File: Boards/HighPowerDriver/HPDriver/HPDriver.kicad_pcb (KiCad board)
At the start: 4 copper layers, 100 parts, among them J1 USB_B_Mini, J2 60V_In, J3 Coils, J4 Screw_Terminal_01x06, J5 AVR-ISP-6, Q10 IRF9530, Q11 BC817, Q12 BC817, Q13 BC817, Q14 BC817, Q9 BC817, SW1 SW_Push, U1 LM5009MM, U10 ATtiny2313A-SU, U2 TMC262, U3 FT230XS, U4 SFH617A-1, U5 SFH617A-1, U6 TLP118, U7 LTV-827S, U8 LTV-827S, U9 74HC14, X1 16MHz, Y1 20MHz

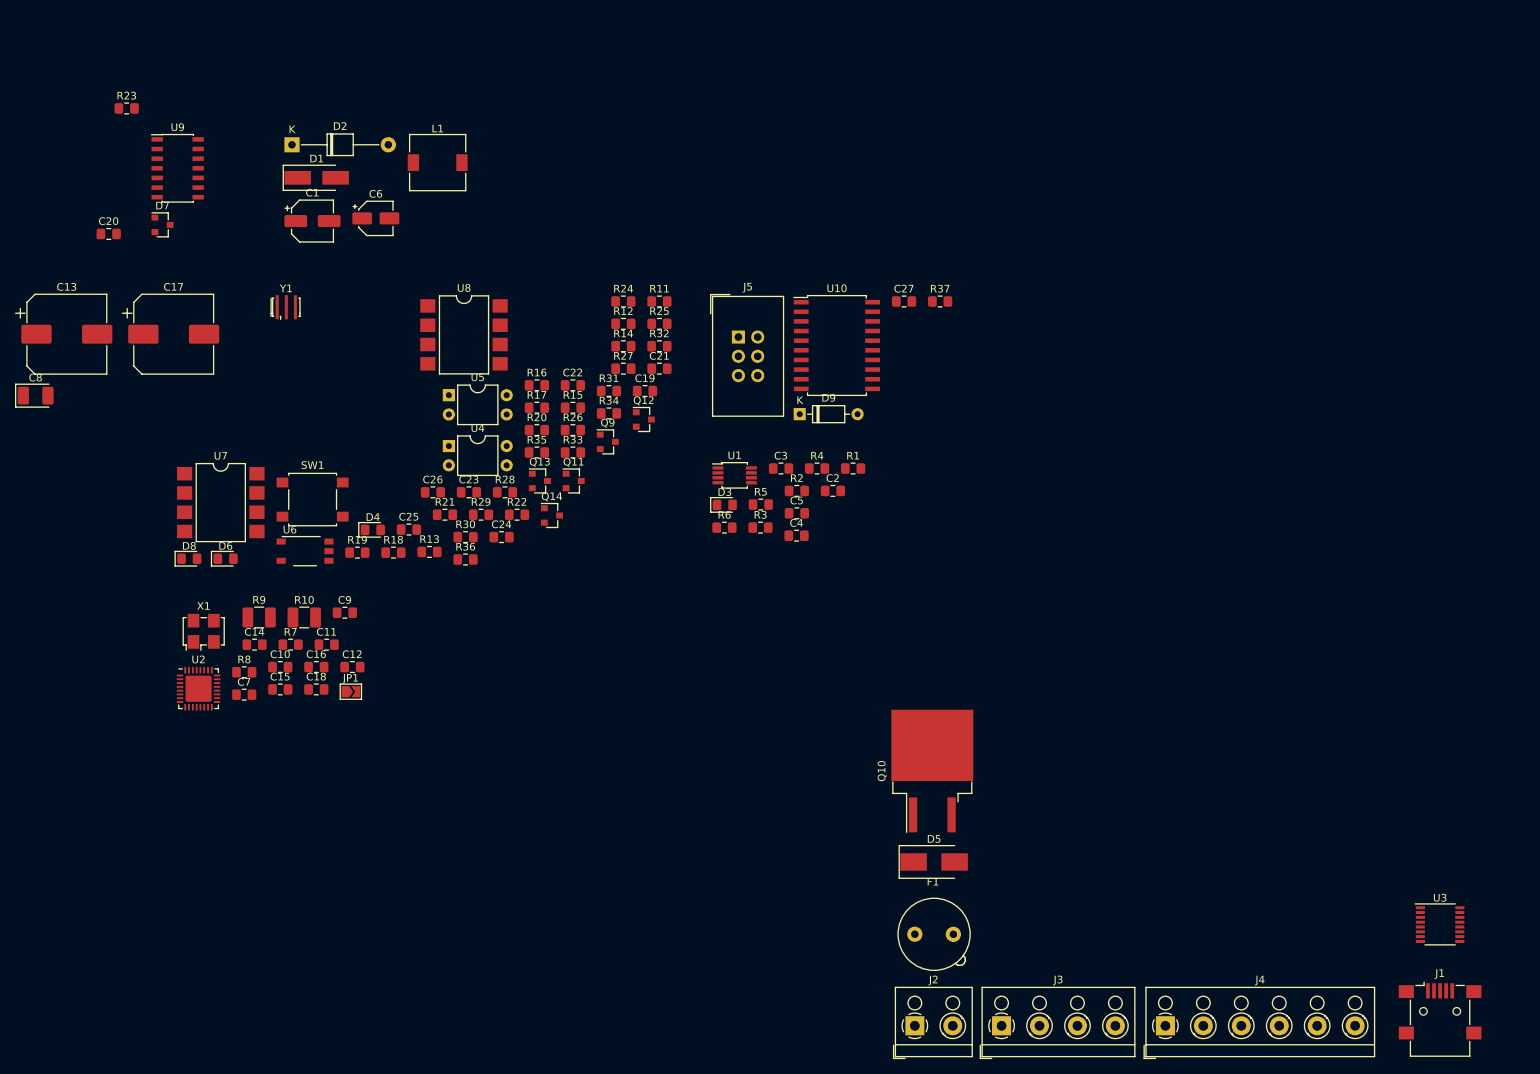
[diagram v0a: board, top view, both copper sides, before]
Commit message: Selected FETs
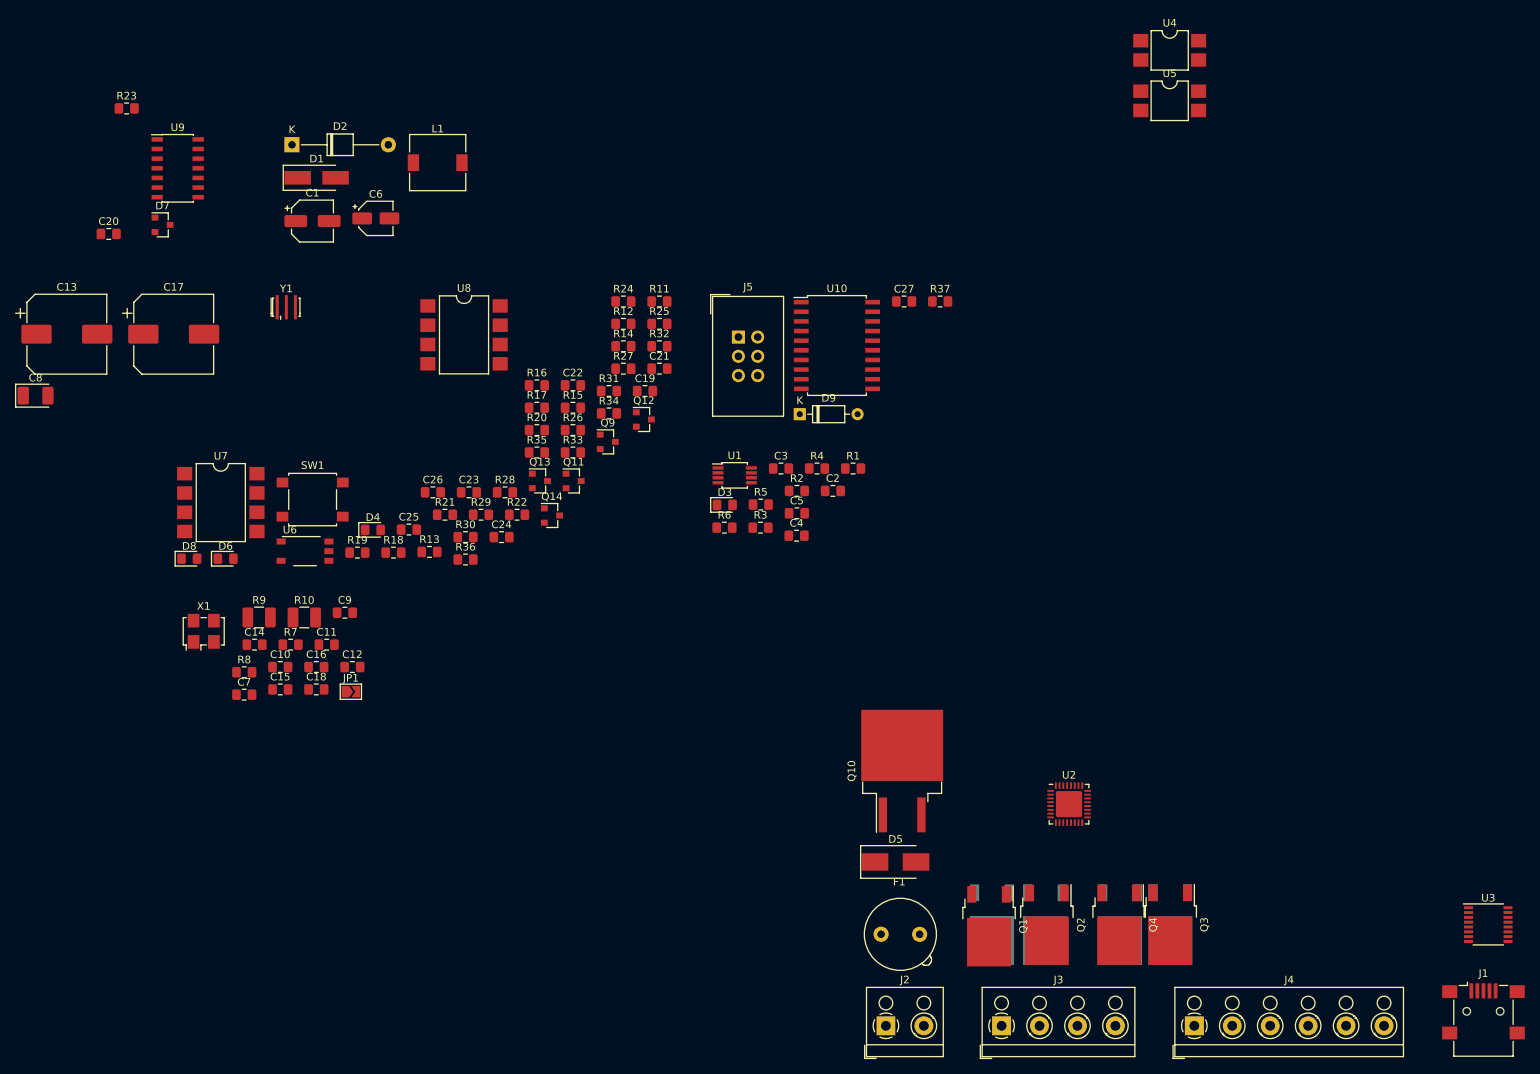
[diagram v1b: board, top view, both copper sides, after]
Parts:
- added Q1: IRFR5410, Package_TO_SOT_SMD:TO-252-2, F.Cu at (138.7, 124.0)
- added Q2: IRFR3910, Package_TO_SOT_SMD:TO-252-2, F.Cu at (146.3, 123.9)
- added Q3: IRFR3910, Package_TO_SOT_SMD:TO-252-2, F.Cu at (162.6, 123.8)
- added Q4: IRFR5410, Package_TO_SOT_SMD:TO-252-2, F.Cu at (155.8, 123.9)
- added Q5: IRFR5410, Package_TO_SOT_SMD:TO-252-2, B.Cu at (146.1, 123.8)
- added Q6: IRFR3910, Package_TO_SOT_SMD:TO-252-2, B.Cu at (139.1, 123.8)
- added Q7: IRFR3910, Package_TO_SOT_SMD:TO-252-2, B.Cu at (156.0, 123.8)
- added Q8: IRFR5410, Package_TO_SOT_SMD:TO-252-2, B.Cu at (162.6, 123.8)
- R23: value (none) -> 380R
- R25: value R -> 380R
- U4, U5: value SFH617A-1 -> SFH6156; footprint Package_DIP:DIP-4_W7.62mm -> Package_DIP:SMDIP-4_W7.62mm
- moved U2 115.7 mm to (149.2, 108.0)
- moved U4 108.4 mm to (162.5, 8.62)
- moved U5 102.6 mm to (162.5, 15.3)
- moved U3 6.35 mm to (204.5, 123.8)
- moved J1 5.72 mm to (203.8, 135.3)
- moved D5 5.08 mm to (126.4, 115.6)
- moved F1 4.45 mm to (124.5, 125.1)
- moved Q10 3.98 mm to (127.2, 103.6)
- moved J2 3.81 mm to (125.1, 137.2)
- moved J4 3.81 mm to (165.7, 137.2)
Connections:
- U2 pad 18: (no net) -> Net-(Q3-Pad1)
- U2 pad 19: (no net) -> Net-(Q7-Pad1)
- U2 pad 2: (no net) -> Net-(Q5-Pad1)
- U2 pad 22: (no net) -> Net-(Q4-Pad1)
- U2 pad 23: (no net) -> Net-(Q8-Pad1)
- U2 pad 3: (no net) -> Net-(Q1-Pad1)
- U2 pad 6: (no net) -> Net-(Q2-Pad1)
- U2 pad 7: (no net) -> Net-(Q6-Pad1)

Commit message: Work in Progress
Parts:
- removed F1: Polyfuse, Fuse:Fuseholder_TR5_Littelfuse_No560_No460
- C1: footprint Capacitor_SMD:CP_Elec_5x5.8 -> Capacitor_SMD:C_1210_3225Metric_Pad1.42x2.65mm_HandSolder
- C6: footprint Capacitor_SMD:CP_Elec_4x4.5 -> Capacitor_SMD:C_1210_3225Metric_Pad1.42x2.65mm_HandSolder
- Q1, Q2, Q3, Q4: moved to B.Cu
- Q10: value IRF9530 -> IRF4950S
- moved R23 182.2 mm to (179.1, 113.7), turned to 270 degrees
- moved C20 169.0 mm to (167.0, 120.7), turned to 270 degrees
- moved U9 142.7 mm to (147.3, 108.0), turned to 90 degrees
- moved C23 121.5 mm to (177.2, 124.5)
- moved U7 121.2 mm to (147.3, 119.4), turned to 90 degrees
- moved R12 117.7 mm to (174.0, 127.6), turned to 270 degrees
- moved R14 117.0 mm to (175.9, 127.6), turned to 270 degrees
- moved C24 116.3 mm to (181.0, 119.4), turned to 90 degrees
- moved Y1 115.3 mm to (152.4, 87.0), turned to 90 degrees
- moved U8 115.0 mm to (158.1, 119.4), turned to 270 degrees
- moved R21 114.1 mm to (172.1, 114.3)
- moved C17 113.9 mm to (132.1, 99.1), turned to 90 degrees
- moved C8 110.1 mm to (113.8, 98.6), turned to 180 degrees
- moved C22 109.3 mm to (169.5, 120.7), turned to 270 degrees
- moved C19 108.1 mm to (170.8, 128.9), turned to 180 degrees
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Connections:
- J2 pad 2: Net-(F1-Pad2) -> Net-(D5-Pad1)
- Q10 pad 1: Net-(D5-Pad1) -> Net-(D7-Pad2)
- Q10 pad 2: Net-(D7-Pad2) -> Net-(D5-Pad1)
- R20 pad 1: /Connector/Enable -> /Driver/DriveEN
- U8 pad 1: Net-(R33-Pad2) -> Net-(R34-Pad2)
- U8 pad 3: Net-(R34-Pad2) -> Net-(R33-Pad2)
- U8 pad 6: Net-(R31-Pad1) -> Net-(R30-Pad1)
- U8 pad 8: Net-(R30-Pad1) -> Net-(R31-Pad1)
- U9 pad 6: /Connector/Enable -> /Driver/DriveEN
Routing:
- net /Connector/Stall: track 0.00 -> 51.9 mm
- net +5V: track 0.00 -> 51.3 mm, vias 0 -> 2
- net +48V: track 0.00 -> 47.6 mm, vias 0 -> 63
- net /Driver/DriveEN: track 0.00 -> 47.1 mm, vias 0 -> 2
- net Net-(Q5-Pad1): track 0.00 -> 46.5 mm, vias 0 -> 1
- net /Connector/Rx: track 0.00 -> 33.9 mm, vias 0 -> 2
- net /Connector/Tx: track 0.00 -> 27.6 mm, vias 0 -> 2
- net Net-(Q1-Pad1): track 0.00 -> 24.8 mm, vias 0 -> 1
- net Net-(C24-Pad1): track 0.00 -> 24.6 mm, vias 0 -> 2
- net /Connector/Reset: track 0.00 -> 23.0 mm
- net Net-(C19-Pad1): track 0.00 -> 22.5 mm, vias 0 -> 2
- net GNDS: track 0.00 -> 21.5 mm, vias 0 -> 18
- net Net-(Q8-Pad1): track 0.00 -> 19.2 mm, vias 0 -> 1
- net Net-(JP1-Pad1): track 0.00 -> 19.0 mm, vias 0 -> 2
- net Net-(Q2-Pad1): track 0.00 -> 17.8 mm, vias 0 -> 1
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- added copper zone on B.Cu, net +48V
- added copper zone on F.Cu, net +48V
- added copper zone on In1.Cu, net +48V
- added copper zone on In2.Cu, net +48V
- added copper zone on F.Cu, net +5V
- added copper zone on B.Cu, net /Connector/Coil_A1
- added copper zone on In1.Cu, net /Connector/Coil_A1
- added copper zone on B.Cu, net /Connector/Coil_A2
- added copper zone on In1.Cu, net /Connector/Coil_A2
- added copper zone on B.Cu, net /Connector/Coil_B1
- added copper zone on In1.Cu, net /Connector/Coil_B1
- added copper zone on B.Cu, net /Connector/Coil_B2
- added copper zone on In1.Cu, net /Connector/Coil_B2
- added copper zone on B.Cu, net GND
- added copper zone on F.Cu, net GND
- added copper zone on In1.Cu, net GND
- added copper zone on In2.Cu, net GND
- added copper zone on F.Cu, net GNDA
- added copper zone on B.Cu, net GNDS
- added copper zone on F.Cu, net GNDS
- added copper zone on B.Cu, net Net-(C14-Pad1)
- added copper zone on F.Cu, net Net-(C14-Pad1)
- added copper zone on In2.Cu, net Net-(C14-Pad1)
- added copper zone on B.Cu, net Net-(C15-Pad1)
- added copper zone on F.Cu, net Net-(C15-Pad1)
- added copper zone on In2.Cu, net Net-(C15-Pad1)
- added copper zone on F.Cu, net Net-(C3-Pad2)
- added copper zone on F.Cu, net Net-(C6-Pad1)
- added copper zone on F.Cu, net Net-(D5-Pad1)
- added copper zone on In1.Cu, net Net-(D5-Pad1)
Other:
- net class Coils removed
- net class DigSupply removed
- net class PowerIn removed

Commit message: Updated Layout
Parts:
- added D10: LED_Gn, LED_SMD:LED_0805_2012Metric_Pad1.15x1.40mm_HandSolder, F.Cu at (140.2, 72.4)
- added D11: LED_Rt, LED_SMD:LED_0805_2012Metric_Pad1.15x1.40mm_HandSolder, F.Cu at (135.9, 72.4)
- added R38: 180R, Resistor_SMD:R_0805_2012Metric_Pad1.15x1.40mm_HandSolder, F.Cu at (140.3, 67.9)
- added R39: 180R, Resistor_SMD:R_0805_2012Metric_Pad1.15x1.40mm_HandSolder, F.Cu at (135.9, 67.9)
- added REF**: MountingHole_2.2mm_M2_Pad, MountingHole:MountingHole_2.2mm_M2_Pad, F.Cu at (180.3, 68.3)
- added REF**: MountingHole_2.2mm_M2_Pad, MountingHole:MountingHole_2.2mm_M2_Pad, F.Cu at (88.4, 68.6)
- added REF**: MountingHole_2.2mm_M2_Pad, MountingHole:MountingHole_2.2mm_M2_Pad, F.Cu at (141.5, 96.5)
- added REF**: MountingHole_2.2mm_M2_Pad, MountingHole:MountingHole_2.2mm_M2_Pad, F.Cu at (180.8, 127.8)
- added REF**: MountingHole_2.2mm_M2_Pad, MountingHole:MountingHole_2.2mm_M2_Pad, F.Cu at (130.8, 135.9)
- added REF**: MountingHole_2.2mm_M2_Pad, MountingHole:MountingHole_2.2mm_M2_Pad, F.Cu at (103.6, 135.9)
- moved D2 24.9 mm to (114.8, 82.0)
- moved R32 21.5 mm to (148.6, 111.0), turned to 90 degrees
- moved C26 14.8 mm to (152.9, 97.3), turned to 90 degrees
- moved R35 14.2 mm to (143.5, 111.0)
- moved D3 11.4 mm to (144.8, 72.4)
- moved R6 10.2 mm to (144.8, 67.9), turned to 270 degrees
- moved Q12 9.94 mm to (127.0, 77.5)
- moved R20 9.94 mm to (127.0, 80.6)
- moved J5 7.47 mm to (169.9, 70.6)
- moved R18 7.12 mm to (153.2, 67.1)
- moved SW1 7.12 mm to (153.1, 72.3)
- moved U9 4.93 mm to (150.1, 103.9), turned to 0 degrees
- moved R36 4.44 mm to (147.3, 97.2)
- moved C10 3.81 mm to (118.7, 84.5)
- moved C12 3.81 mm to (120.9, 84.5)
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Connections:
- U10 pad 14: (no net) -> /Connector/Error
- U10 pad 15: (no net) -> /Connector/Active
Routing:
- net /Connector/Step: track 0.00 -> 76.3 mm, vias 0 -> 6
- net /Connector/Ready: track 0.00 -> 70.1 mm, vias 0 -> 4
- net /Connector/Error: track 0.00 -> 69.1 mm, vias 0 -> 3
- net /Controller/MISO: track 12.9 -> 79.7 mm, vias 0 -> 2
- net /Connector/Dir: track 0.00 -> 65.8 mm, vias 0 -> 4
- net /Controller/SCK: track 15.0 -> 78.9 mm, vias 2 -> 3
- net /Controller/MOSI: track 12.1 -> 74.4 mm, vias 0 -> 2
- net /Connector/Active: track 0.00 -> 61.1 mm, vias 0 -> 3
- net /Controller/CS_TMC: track 0.00 -> 52.3 mm, vias 0 -> 2
- net /Connector/Coil_A1: track 0.00 -> 51.4 mm, vias 19 -> 31
- net /Connector/Coil_B2: track 0.00 -> 50.2 mm, vias 24 -> 26
- net Net-(Q3-Pad1): track 0.00 -> 48.5 mm, vias 0 -> 1
- net Net-(Q6-Pad1): track 0.00 -> 47.9 mm, vias 0 -> 3
- net Net-(Q4-Pad1): track 0.00 -> 40.7 mm, vias 0 -> 1
- net /Connector/Stall: track 51.9 -> 86.2 mm, vias 0 -> 6
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- added copper zone on In1.Cu, net +5V
- added copper zone on In1.Cu, net GNDS
- added copper zone on In2.Cu, net GNDS
- removed copper zone on In1.Cu, net GND
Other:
- board outline added: 100.6 x 76.2 mm

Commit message: Update HPDriver.kicad_pcb
Layout update
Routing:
- net /Connector/Coil_B2: track 50.2 -> 45.0 mm, vias 26 -> 25
- net Net-(Q5-Pad1): track 44.7 -> 49.6 mm
- net /Connector/Rx: track 36.0 -> 32.5 mm
- net Net-(Q6-Pad1): track 47.9 -> 44.7 mm
- net /Controller/MOSI: track 74.4 -> 77.2 mm
- net /Controller/MISO: track 79.7 -> 82.4 mm
- net /Controller/SCK: track 78.9 -> 81.5 mm
- net /Controller/CS_TMC: track 52.3 -> 54.7 mm
- net /Driver/DriveEN: track 77.9 -> 80.2 mm
- net Net-(Q3-Pad1): track 48.5 -> 46.8 mm
- net +5V: track 78.2 -> 79.7 mm
- net /Connector/Tx: track 29.2 -> 27.8 mm
- net Net-(C24-Pad1): track 25.1 -> 23.7 mm
- net /Connector/Coil_A2: track 26.7 -> 27.9 mm, vias 33 -> 20
- net Net-(Q1-Pad1): track 24.6 -> 25.4 mm
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
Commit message: Update HPDriver.kicad_pcb
Layout update
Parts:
- moved C7 0.85 mm to (134.1, 88.9)
- moved X1 0.54 mm to (130.0, 88.6)
- moved JP1 0.51 mm to (129.8, 84.3)
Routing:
- net +48V: track 81.8 -> 98.7 mm
- net Net-(Q5-Pad1): track 49.6 -> 42.6 mm
- net Net-(Q3-Pad1): track 46.8 -> 51.5 mm
- net Net-(Q6-Pad1): track 44.7 -> 48.4 mm
- net Net-(Q4-Pad1): track 40.8 -> 43.9 mm
- net /Controller/MOSI: track 77.2 -> 74.4 mm
- net /Controller/MISO: track 82.4 -> 79.7 mm
- net /Controller/SCK: track 81.5 -> 79.1 mm
- net /Controller/CS_TMC: track 54.7 -> 52.5 mm
- net Net-(Q2-Pad1): track 20.1 -> 22.0 mm
- net /Connector/Coil_B2: track 45.0 -> 46.8 mm
- net /Connector/Step: track 76.3 -> 77.9 mm
- net +5V: track 79.7 -> 78.1 mm
- net /Connector/Coil_A2: track 27.9 -> 29.3 mm
- net Net-(Q1-Pad1): track 25.4 -> 26.7 mm
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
